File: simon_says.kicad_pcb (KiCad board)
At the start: 2 copper layers, 97 x 60 mm, 19 parts, among them SW1 SW_Push_LED, SW2 SW_Push_LED, SW3 SW_Push_LED, SW4 SW_Push_LED, U1 ATtiny25-20P

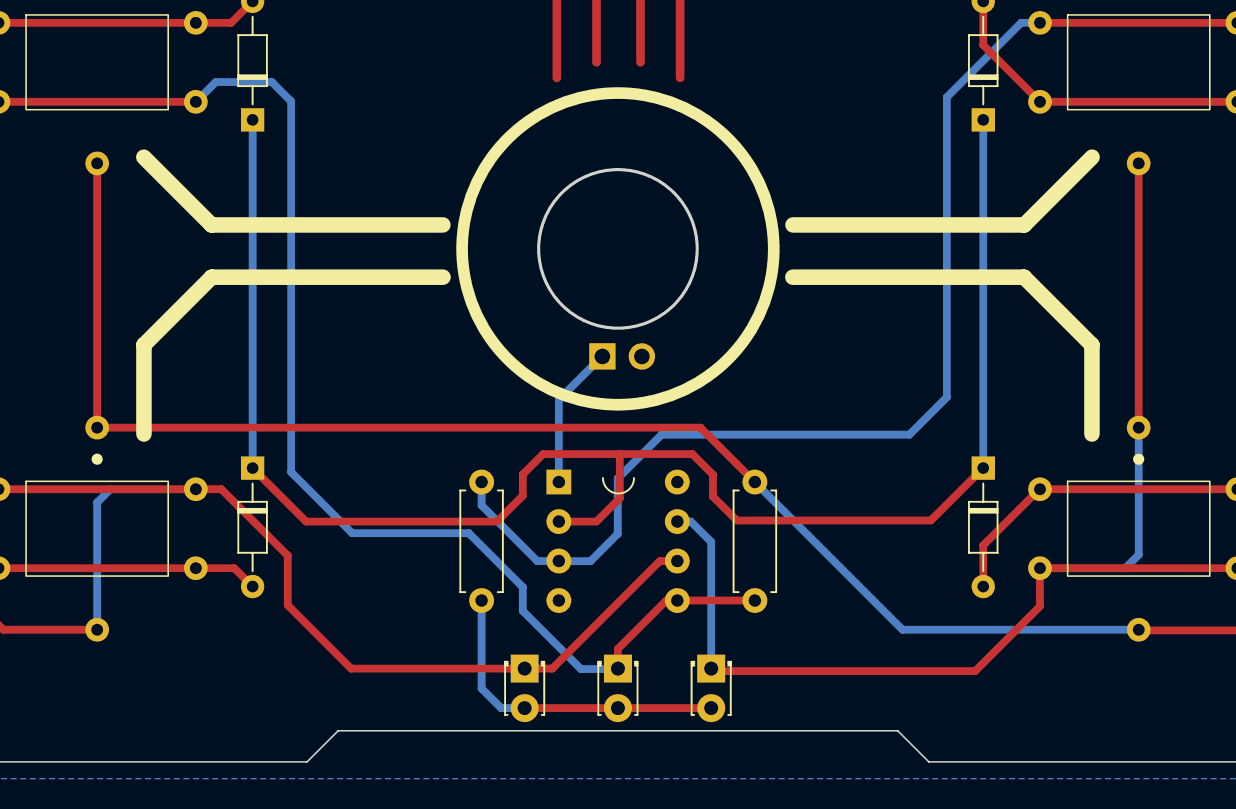
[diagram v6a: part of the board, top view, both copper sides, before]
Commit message: Optimized routing and removed component outlines
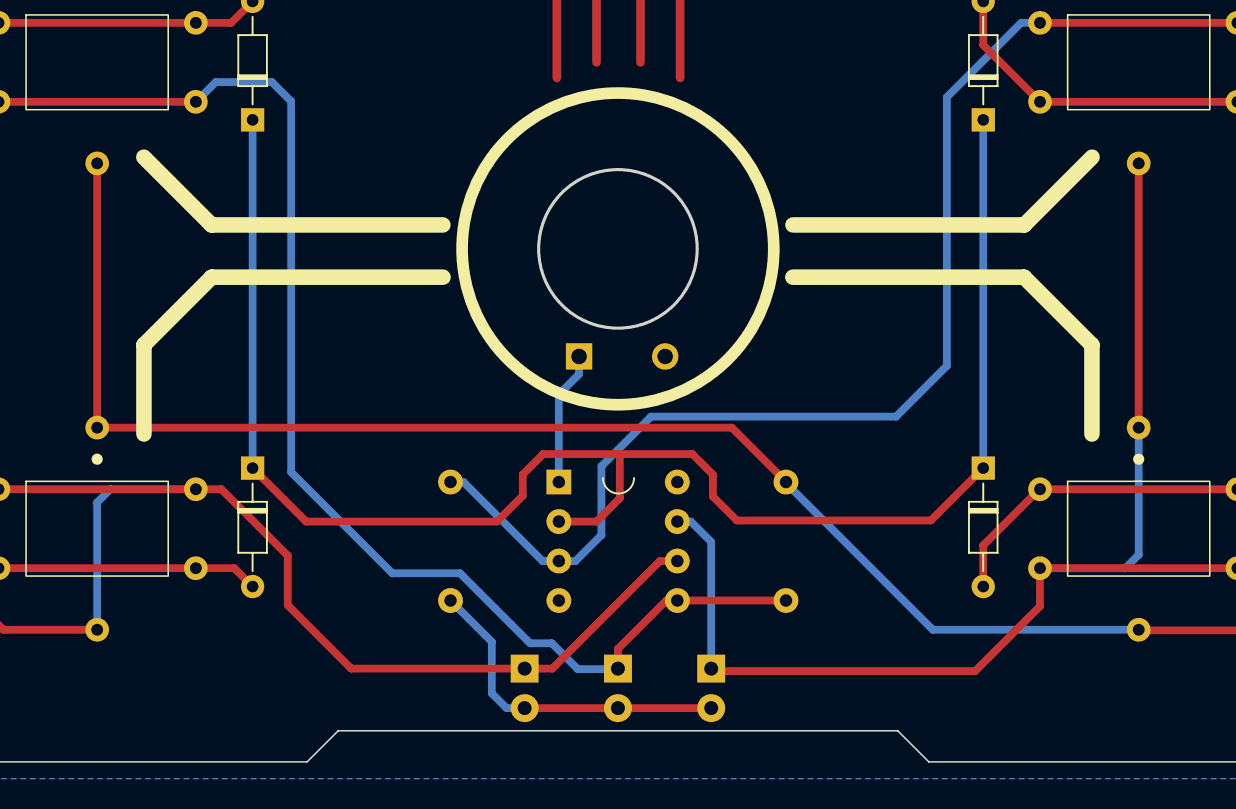
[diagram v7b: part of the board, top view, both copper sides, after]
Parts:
- moved R1 2.00 mm to (109.3, 149.6)
- moved R2 2.00 mm to (87.7, 142.0)
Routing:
- net MM1: track 82.3 -> 83.4 mm
- net SPK: track 9.25 -> 8.62 mm
- net Net-(D10-A): track 21.0 -> 21.6 mm

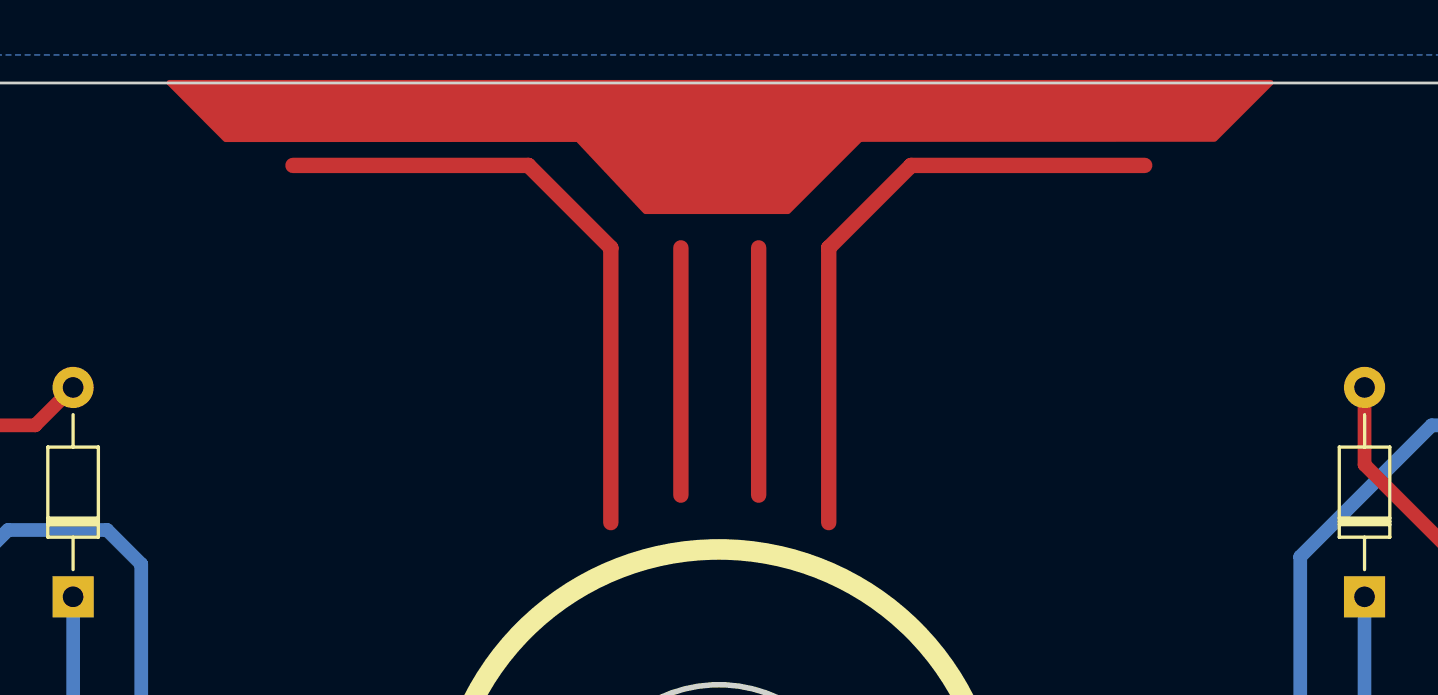
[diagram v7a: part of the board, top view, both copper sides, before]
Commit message: Finilized front face
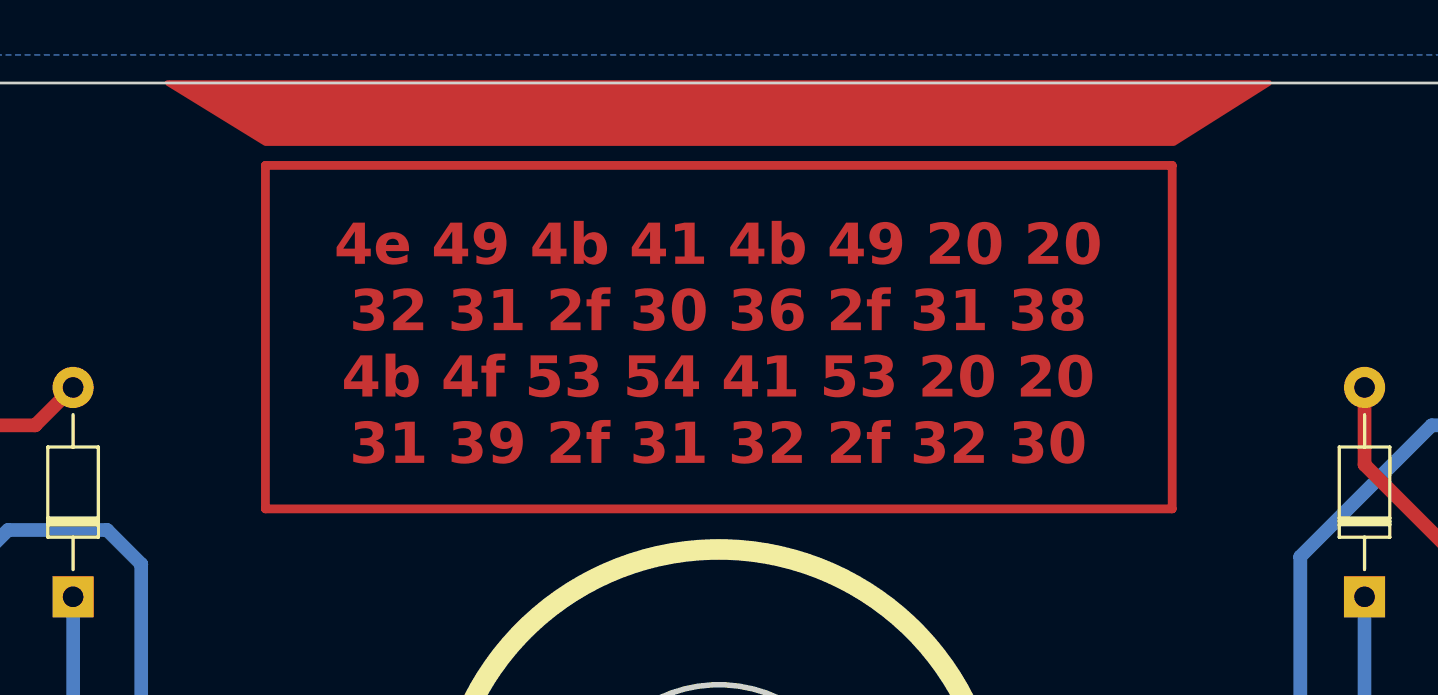
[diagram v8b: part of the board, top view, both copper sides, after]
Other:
- board text added: "4e 49 4b 41 4b 49 20 20 32 31 2f 30 36 2f 31 38 4b 4f 53 54 41 53 20 20 31 39 2f 31 32 2f 32 30"
